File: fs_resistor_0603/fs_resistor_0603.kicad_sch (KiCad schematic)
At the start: 3 parts

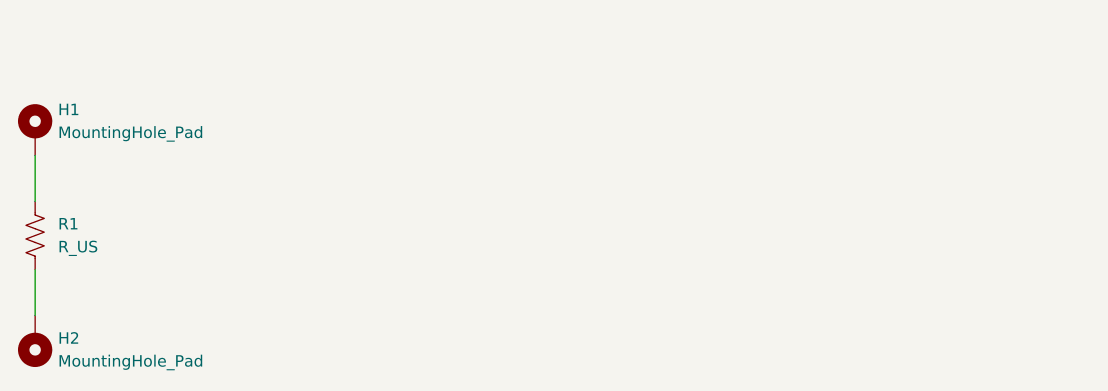
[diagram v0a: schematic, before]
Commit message: resistor 0603 stitch breakout board
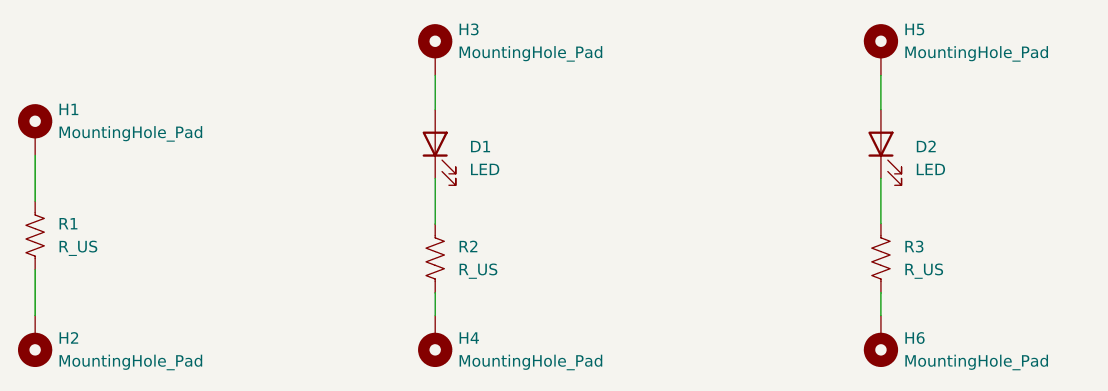
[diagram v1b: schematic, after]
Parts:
- added D1: LED, Diode_SMD:D_0603_1608Metric_Pad1.05x0.95mm_HandSolder, symbol Device:LED
- added D2: LED, LED_SMD:LED_0805_2012Metric_Pad1.15x1.40mm_HandSolder, symbol Device:LED
- added H3, H4, H5, H6: MountingHole_Pad, MountingHole:MountingHole_2.2mm_M2_DIN965_Pad_TopBottom, symbol Mechanical:MountingHole_Pad
- added R2: R_US, Resistor_SMD:R_0603_1608Metric_Pad0.98x0.95mm_HandSolder, symbol Device:R_US
- added R3: R_US, Resistor_SMD:R_0805_2012Metric_Pad1.20x1.40mm_HandSolder, symbol Device:R_US
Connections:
- new net: D1.1 (K), R2.1
- new net: D1.2 (A), H3.1
- new net: D2.1 (K), R3.1
- new net: D2.2 (A), H5.1
- new net: H6.1, R3.2
- new net: H4.1, R2.2
